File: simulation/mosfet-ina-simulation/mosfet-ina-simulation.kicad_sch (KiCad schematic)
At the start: 0 parts

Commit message: simulation double opamp
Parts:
- added C1, C2, C4: 100n, symbol Device:C
- added C3: 10n, symbol Device:C
- added L1: 50u, symbol Device:L
- added Q1: NMOS, symbol Simulation_SPICE:NMOS
- added R1, R2: 1k, symbol Device:R
- added R3, R4: 100k, symbol Device:R
- added R5: 500, symbol Device:R
- added R6: 100, symbol Device:R
- added R7: 10k, symbol Device:R
- added Rs1: 100m, symbol Device:R
- added U1, U2: ${SIM.PARAMS}, symbol Simulation_SPICE:OPAMP
- added V1: 5, symbol Simulation_SPICE:VDC
- added V2: 50m, symbol Simulation_SPICE:VDC
- added V3: 12, symbol Simulation_SPICE:VDC
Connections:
- new net: C3.2, R5.1, U2.2 (-)
- new net: C3.1, R6.1, U2.5
- new net: Q1.2 (G), R6.2, R7.2
- new net: R2.1, R3.2, U1.2 (-)
- new net: C4.2, L1.2, Q1.1 (D)
- new net: R1.1, R4.2, U1.1 (+)
- new net +12V: C1.2, C2.2, U1.3 (V+), U2.3 (V+), V3.1
- new net GND: C1.1, C2.1, C4.1, R2.2, R4.1, R7.1, Rs1.1, U1.4 (V-), U2.4 (V-), V1.2, V2.2, V3.2
- new net V_I_CTRL: U2.1 (+), V1.1
- new net batt+: L1.1, V2.1
- new net out: R3.1, R5.2, U1.5
- new net shunt_p: Q1.3 (S), R1.2, Rs1.2
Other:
- note added: "*.TRAN TSTEP TSTOP <TSTART <TMAX>> <UIC>"
- note added: ".tran 10u 10m 0"

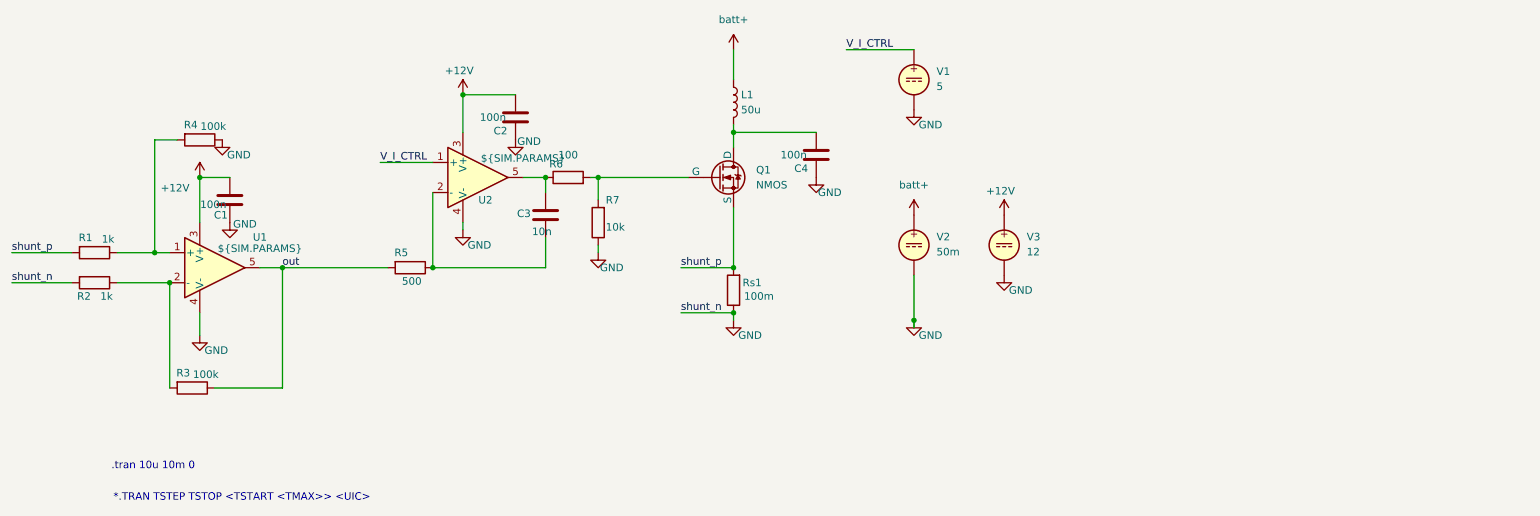
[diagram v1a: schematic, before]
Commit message: First try of two stage opa
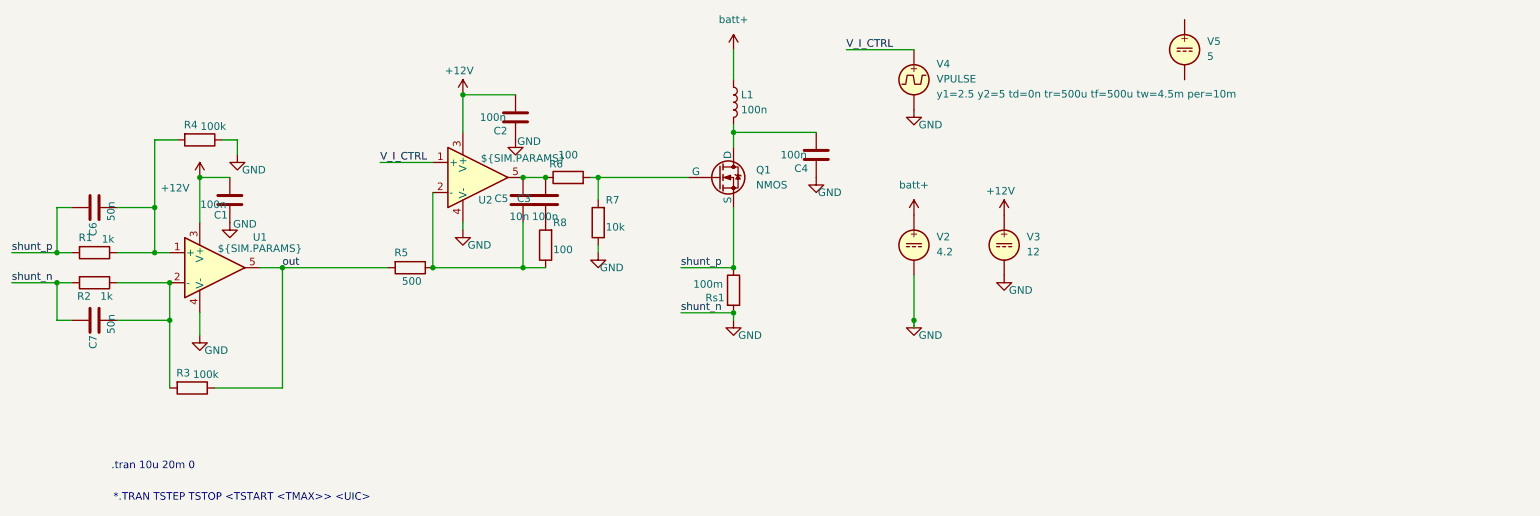
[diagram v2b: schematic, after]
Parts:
- removed V1: 5, symbol Simulation_SPICE:VDC
- added C5: 10n, symbol Device:C
- added C6, C7: 50n, symbol Device:C
- added R8: 100, symbol Device:R
- added V4: VPULSE, symbol Simulation_SPICE:VPULSE
- added V5: 5, symbol Simulation_SPICE:VDC
- C3: value 10n -> 100n
- L1: value 50u -> 100n
- V2: value 50m -> 4.2
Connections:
- net GND: now also Rs1.2, C7.1, V4.2; no longer Rs1.1
- net V_I_CTRL: now also V4.1
- net shunt_p: now also Rs1.1, C6.1; no longer Rs1.2
- net at R5.1, U2.2 (-): now also C5.2, R8.1; no longer C3.2
- net at C3.1, R6.1, U2.5: now also C5.1
- net at R2.1, R3.2, U1.2 (-): now also C7.2
- net at R1.1, R4.2, U1.1 (+): now also C6.2
- new net: C3.2, R8.2
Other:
- note added: ".tran 10u 20m 0"
- note removed: ".tran 10u 10m 0"
- moved on the sheet: C3, Rs1

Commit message: ac analysis
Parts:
- added V1: VSIN, symbol Simulation_SPICE:VSIN
- V5: value 5 -> 1
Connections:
- net GND: now also V5.2, V1.2; no longer V4.2
- net V_I_CTRL: now also V5.1; no longer V4.1
- net at C6.2, R1.1, R4.2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: now also V1.1
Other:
- moved on the sheet: V4, V5
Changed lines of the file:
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@@
+	(wire
+		(pts
+			(xy 55.88 86.36) (xy 55.88 64.77)
+		)
+		(stroke
+			(width 0)
+			(type default)
+		)
+	)
 	(wire
 		(pts
@@
 		(pts
 			(xy 172.72 30.48) (xy 184.15 30.48)
+		)
+		(stroke
+			(width 0)
+			(type default)
+		)
+	)
+	(wire
+		(pts
+			(xy 36.83 86.36) (xy 55.88 86.36)
 		)
 		(stroke
@@
 	)
 	(symbol
+		(lib_id "Simulation_SPICE:VSIN")
+		(at 36.83 91.44 0)
+		(unit 1)
+		(exclude_from_sim no)
+		(in_bom yes)
+		(on_board yes)
+		(dnp no)
+		(fields_autoplaced yes)
+		(property "Reference" "V1"
+			(at 40.64 88.7701 0)
+			(effects
+				(font
+					(size 1.27 1.27)
+				)
+				(justify left)
+			)
+		)
+		(property "Value" "VSIN"
+			(at 40.64 91.3101 0)
+			(effects
+				(font
+					(size 1.27 1.27)
+				)
+				(justify left)
+			)
+		)
+		(property "Footprint" ""
+			(at 36.83 91.44 0)
+			(effects
+				(font
+					(size 1.27 1.27)
+				)
+				(hide yes)
+			)
+		)
+		(property "Datasheet" "https://ngspice.sourceforge.io/docs/ngspice-html-manual/manual.xhtml#sec_Independent_Sources_for"
+			(at 36.83 91.44 0)
+			(effects
+				(font
+					(size 1.27 1.27)
+				)
+				(hide yes)
+			)
+		)
+		(property "Description" "Voltage source, sinusoidal"
+			(at 36.83 91.44 0)
+			(effects
+				(font
+					(size 1.27 1.27)
+				)
+				(hide yes)
+			)
+		)
+		(property "Sim.Pins" "1=+ 2=-"
+			(at 36.83 91.44 0)
+			(effects
+				(font
+					(size 1.27 1.27)
+				)
+				(hide yes)
+			)
+		)
+		(property "Sim.Params" "dc=0 ampl=1 f=1k ac=1"
+			(at 40.64 93.8501 0)
+			(effects
+				(font
+					(size 1.27 1.27)
+				)
+				(justify left)
+			)
+		)
+		(property "Sim.Type" "SIN"
+			(at 36.83 91.44 0)
+			(effects
+				(font
+					(size 1.27 1.27)
+				)
+				(hide yes)
+			)
+		)
+		(property "Sim.Device" "V"
+			(at 36.83 91.44 0)
+			(effects
+				(font
+					(size 1.27 1.27)
+				)
+				(justify left)
+				(hide yes)
+			)
+		)
+		(pin "2"
+		)
+		(pin "1"
+		)
+		(instances
+			(project "mosfet-ina-simulation"
+				(path "/c153c308-03e0-4d4b-a368-42bad221d52c"
+					(reference "V1")
+					(unit 1)
+				)
+			)
+		)
+	)
+	(symbol
 		(lib_id "Simulation_SPICE:OPAMP")
 		(at 110.49 52.07 0)
@@
 				(path "/c153c308-03e0-4d4b-a368-42bad221d52c"
 					(reference "R6")
+					(unit 1)
+				)
+			)
+		)
+	)
+	(symbol
+		(lib_id "power:GND")
+		(at 36.83 96.52 0)
+		(unit 1)
+		(exclude_from_sim no)
+		(in_bom yes)
+		(on_board yes)
+		(dnp no)
+		(fields_autoplaced yes)
+		(property "Reference" "#PWR017"
+			(at 36.83 102.87 0)
+			(effects
+				(font
+					(size 1.27 1.27)
+				)
+				(hide yes)
+			)
+		)
+		(property "Value" "GND"
+			(at 36.83 101.6 0)
+			(effects
+				(font
+					(size 1.27 1.27)
+				)
+			)
+		)
+		(property "Footprint" ""
+			(at 36.83 96.52 0)
+			(effects
+				(font
+					(size 1.27 1.27)
+				)
+				(hide yes)
+			)
+		)
+		(property "Datasheet" ""
+			(at 36.83 96.52 0)
+			(effects
+				(font
+					(size 1.27 1.27)
+				)
+				(hide yes)
+			)
+		)
+		(property "Description" "Power symbol creates a global label with name \"GND\" , ground"
+			(at 36.83 96.52 0)
+			(effects
+				(font
+					(size 1.27 1.27)
+				)
+				(hide yes)
+			)
+		)
+		(pin "1"
+		)
+		(instances
+			(project ""
+				(path "/c153c308-03e0-4d4b-a368-42bad221d52c"
+					(reference "#PWR017")
 					(unit 1)
 				)
@@
 	(symbol
 		(lib_id "Simulation_SPICE:VPULSE")
-		(at 184.15 35.56 0)
-		(unit 1)
-		(exclude_from_sim no)
+		(at 219.71 46.99 0)
+		(unit 1)
+		(exclude_from_sim yes)
 		(in_bom yes)
 		(on_board yes)
@@
 		(fields_autoplaced yes)
 		(property "Reference" "V4"
-			(at 187.96 32.8901 0)
+			(at 223.52 44.3201 0)
 			(effects
 				(font
@@
 		)
 		(property "Value" "VPULSE"
-			(at 187.96 35.4301 0)
+			(at 223.52 46.8601 0)
 			(effects
 				(font
@@
 		)
 		(property "Footprint" ""
-			(at 184.15 35.56 0)
+			(at 219.71 46.99 0)
 			(effects
 				(font
@@
 		)
 		(property "Datasheet" "https://ngspice.sourceforge.io/docs/ngspice-html-manual/manual.xhtml#sec_Independent_Sources_for"
-			(at 184.15 35.56 0)
+			(at 219.71 46.99 0)
 			(effects
 				(font
@@
 		)
 		(property "Description" "Voltage source, pulse"
-			(at 184.15 35.56 0)
+			(at 219.71 46.99 0)
 			(effects
 				(font
@@
 		)
 		(property "Sim.Pins" "1=+ 2=-"
-			(at 184.15 35.56 0)
+			(at 219.71 46.99 0)
 			(effects
 				(font
@@
 		)
 		(property "Sim.Type" "PULSE"
-			(at 184.15 35.56 0)
+			(at 219.71 46.99 0)
 			(effects
 				(font
@@
 		)
 		(property "Sim.Device" "V"
-			(at 184.15 35.56 0)
+			(at 219.71 46.99 0)
 			(effects
 				(font
@@
 		)
 		(property "Sim.Params" "y1=2.5 y2=5 td=0n tr=500u tf=500u tw=4.5m per=10m"
-			(at 187.96 37.9701 0)
+			(at 223.52 49.4001 0)
 			(effects
 				(font
@@
 	(symbol
 		(lib_id "Simulation_SPICE:VDC")
-		(at 229.87 30.48 0)
-		(unit 1)
-		(exclude_from_sim yes)
+		(at 184.15 35.56 0)
+		(unit 1)
+		(exclude_from_sim no)
 		(in_bom yes)
 		(on_board yes)
@@
 		(fields_autoplaced yes)
 		(property "Reference" "V5"
-			(at 233.68 29.0801 0)
+			(at 187.96 34.1601 0)
 			(effects
 				(font
@@
 			)
 		)
-		(property "Value" "5"
-			(at 233.68 31.6201 0)
+		(property "Value" "1"
+			(at 187.96 36.7001 0)
 			(effects
 				(font
@@
 		)
 		(property "Footprint" ""
-			(at 229.87 30.48 0)
+			(at 184.15 35.56 0)
 			(effects
 				(font
@@
 		)
 		(property "Datasheet" "https://ngspice.sourceforge.io/docs/ngspice-html-manual/manual.xhtml#sec_Independent_Sources_for"
-			(at 229.87 30.48 0)
+			(at 184.15 35.56 0)
 			(effects
 				(font
@@
 		)
 		(property "Description" "Voltage source, DC"
-			(at 229.87 30.48 0)
+			(at 184.15 35.56 0)
 			(effects
 				(font
@@
 		)
 		(property "Sim.Pins" "1=+ 2=-"
-			(at 229.87 30.48 0)
+			(at 184.15 35.56 0)
 			(effects
 				(font
@@
 		)
 		(property "Sim.Type" "DC"
-			(at 229.87 30.48 0)
+			(at 184.15 35.56 0)
 			(effects
 				(font
@@
 		)
 		(property "Sim.Device" "V"
-			(at 229.87 30.48 0)
-			(effects
-				(font
+			(at 184.15 35.56 0)
+			(effects
+				(font

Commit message: Add simulate parameters
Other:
- note added: "*.AC DEC ND FSTART FSTOP"
- note added: "*.tran 10u 20m 0"
- note added: ".ac DEC 1000 10 10k"
- note removed: ".tran 10u 20m 0"
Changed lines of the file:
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@@
 	(generator_version "9.0")
 	(paper "A4")
-	(text ".tran 10u 20m 0"
+	(text "*.tran 10u 20m 0"
 		(exclude_from_sim no)
 		(at 55.626 100.838 0)
 		(effects
 			(font
+				(size 1.27 1.27)
+			)
+		)
+	)
+	(text "*.AC DEC ND FSTART FSTOP"
+		(exclude_from_sim no)
+		(at 117.602 105.41 0)
+		(effects
+			(font
+				(size 1.27 1.27)
+			)
+		)
+	)
+	(text ".ac DEC 1000 10 10k"
+		(exclude_from_sim no)
+		(at 115.824 101.6 0)
+		(effects
+			(font
